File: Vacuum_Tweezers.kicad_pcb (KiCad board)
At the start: 2 copper layers, 40.2 x 28 mm, 0 parts

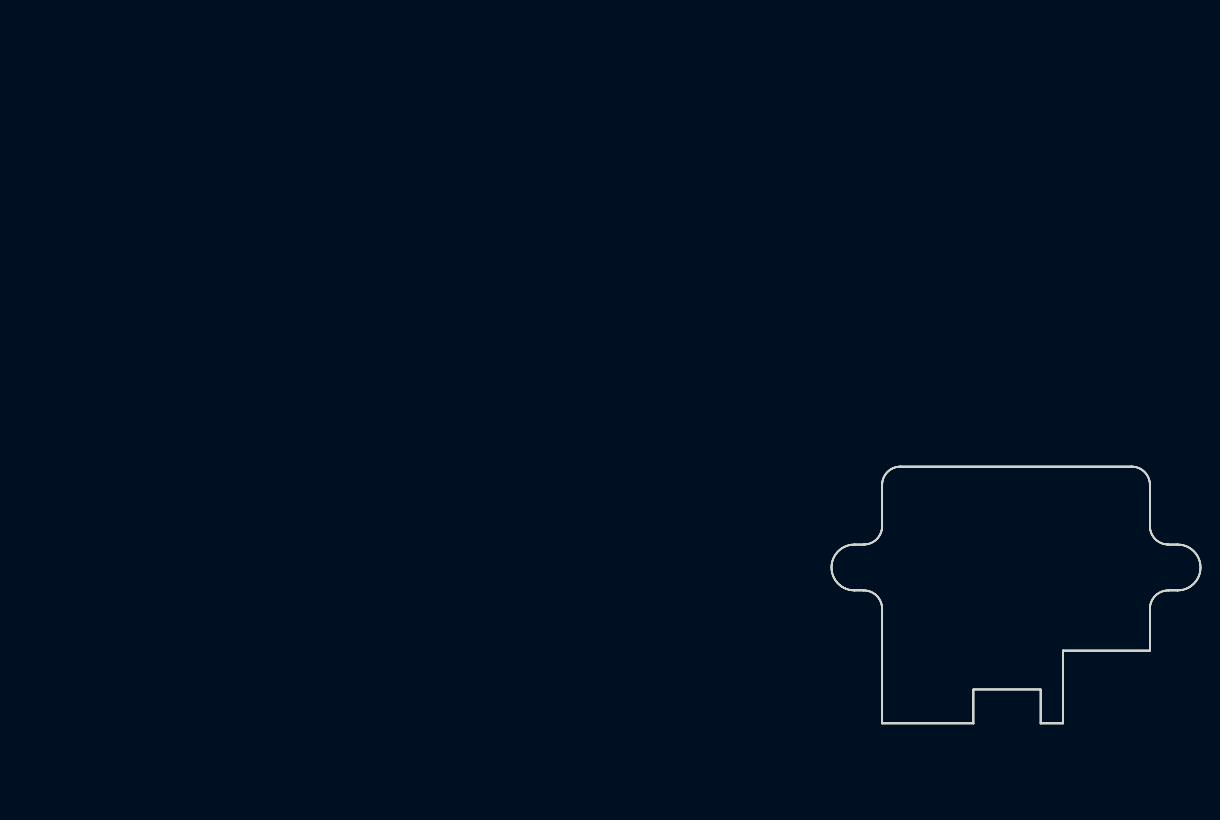
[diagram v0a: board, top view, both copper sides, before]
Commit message: Changed footprints
Modified some footprints to better fit layout and part availability
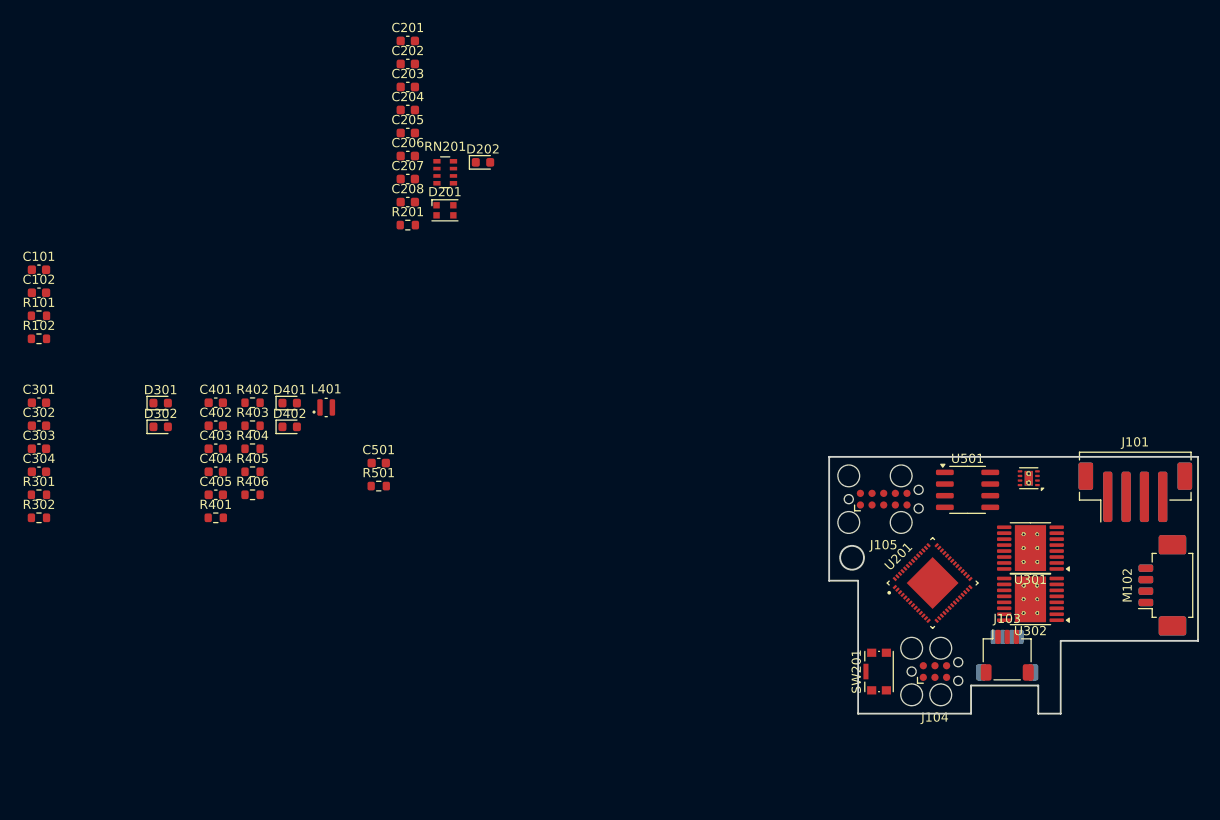
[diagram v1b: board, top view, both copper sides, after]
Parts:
- added C101: 1u, Capacitor_SMD:C_0603_1608Metric, F.Cu at (38.9, 66.2)
- added C102: 1u, Capacitor_SMD:C_0603_1608Metric, F.Cu at (38.9, 68.7)
- added C201: 1u, Capacitor_SMD:C_0603_1608Metric, F.Cu at (79.2, 41.2)
- added C202: 1u, Capacitor_SMD:C_0603_1608Metric, F.Cu at (79.2, 43.7)
- added C203: 1u, Capacitor_SMD:C_0603_1608Metric, F.Cu at (79.2, 46.2)
- added C204: 1u, Capacitor_SMD:C_0603_1608Metric, F.Cu at (79.2, 48.7)
- added C205: 1u, Capacitor_SMD:C_0603_1608Metric, F.Cu at (79.2, 51.3)
- added C206: 1u, Capacitor_SMD:C_0603_1608Metric, F.Cu at (79.2, 53.8)
- added C207: 1u, Capacitor_SMD:C_0603_1608Metric, F.Cu at (79.2, 56.3)
- added C208: 1u, Capacitor_SMD:C_0603_1608Metric, F.Cu at (79.2, 58.8)
- added C301: 10u, Capacitor_SMD:C_0603_1608Metric, F.Cu at (38.9, 80.7)
- added C302: 10u, Capacitor_SMD:C_0603_1608Metric, F.Cu at (38.9, 83.2)
- added C303: 2u2, Capacitor_SMD:C_0603_1608Metric, F.Cu at (38.9, 85.7)
- added C304: 2u2, Capacitor_SMD:C_0603_1608Metric, F.Cu at (38.9, 88.2)
- added C401: 10u, Capacitor_SMD:C_0603_1608Metric, F.Cu at (58.2, 80.7)
- added C402: 10u, Capacitor_SMD:C_0603_1608Metric, F.Cu at (58.2, 83.2)
- added C403: 10u, Capacitor_SMD:C_0603_1608Metric, F.Cu at (58.2, 85.7)
- added C404: 1u, Capacitor_SMD:C_0603_1608Metric, F.Cu at (58.2, 88.2)
- added C405: 1u, Capacitor_SMD:C_0603_1608Metric, F.Cu at (58.2, 90.7)
- added C501: 1u, Capacitor_SMD:C_0603_1608Metric, F.Cu at (76.0, 87.2)
- added D201: WS2812B, LED_SMD:LED_WS2812B-2020_PLCC4_2.0x2.0mm, F.Cu at (83.2, 59.7)
- added D202: LED, Diode_SMD:D_0603_1608Metric, F.Cu at (87.4, 54.5)
- added D301: RED, Diode_SMD:D_0603_1608Metric, F.Cu at (52.2, 80.7)
- added D302: RED, Diode_SMD:D_0603_1608Metric, F.Cu at (52.2, 83.3)
- added D401: RED, LED_SMD:LED_0603_1608Metric, F.Cu at (66.3, 80.7)
- added D402: RED, LED_SMD:LED_0603_1608Metric, F.Cu at (66.3, 83.3)
- added J101: PnP Interface, Connector_JST:JST_PH_B4B-PH-SM4-TB_1x04-1MP_P2.00mm_Vertical, F.Cu at (158.5, 90.4)
- added J102: Magnetic Encoder, Connector_JST:JST_SH_SM04B-SRSS-TB_1x04-1MP_P1.00mm_Horizontal, B.Cu at (144.5, 108.2)
- added J103: Limit Switch, Connector_JST:JST_SH_SM03B-SRSS-TB_1x03-1MP_P1.00mm_Horizontal, F.Cu at (144.5, 108.2)
- added J104: TC2030 PROG, Connector:Tag-Connect_TC2030-IDC-FP_2x03_P1.27mm_Vertical, F.Cu at (136.7, 110.0)
- added J105: TC2050 JTAG, Connector:Tag-Connect_TC2050-IDC-FP_2x05_P1.27mm_Vertical, F.Cu at (131.1, 91.2)
- added J106: PnP Interface, Connector_JST:JST_PH_B4B-PH-SM4-TB_1x04-1MP_P2.00mm_Vertical, B.Cu at (158.5, 90.4)
- added L401: 2u2, Inductor_SMD:L_Coilcraft_XFL2010, F.Cu at (70.3, 81.2)
- added M101: Z-Axis, Connector_Molex:Molex_PicoBlade_53261-0471_1x04-1MP_P1.25mm_Horizontal, B.Cu at (162.1, 100.6)
- added M102: C-Axis, Connector_Molex:Molex_PicoBlade_53261-0471_1x04-1MP_P1.25mm_Horizontal, F.Cu at (162.1, 100.6)
- added R101: 100R, Resistor_SMD:R_0603_1608Metric, F.Cu at (38.9, 71.2)
- added R102: 100R, Resistor_SMD:R_0603_1608Metric, F.Cu at (38.9, 73.7)
- added R201: 1k, Resistor_SMD:R_0603_1608Metric, F.Cu at (79.2, 61.3)
- added R301: 1k, Resistor_SMD:R_0603_1608Metric, F.Cu at (38.9, 90.7)
- added R302: 1k, Resistor_SMD:R_0603_1608Metric, F.Cu at (38.9, 93.2)
- added R401: 100k, Resistor_SMD:R_0603_1608Metric, F.Cu at (58.2, 93.2)
- added R402: 100R, Resistor_SMD:R_0603_1608Metric, F.Cu at (62.2, 80.7)
- added R403: 1k, Resistor_SMD:R_0603_1608Metric, F.Cu at (62.2, 83.2)
- added R404: 3k0, Resistor_SMD:R_0603_1608Metric, F.Cu at (62.2, 85.7)
- added R405: 1k, Resistor_SMD:R_0603_1608Metric, F.Cu at (62.2, 88.2)
- added R406: 430R, Resistor_SMD:R_0603_1608Metric, F.Cu at (62.2, 90.7)
- added R501: 120R, Resistor_SMD:R_0603_1608Metric, F.Cu at (76.0, 89.8)
- added RN201: 10k, Resistor_SMD:R_Array_Convex_4x0603, F.Cu at (83.2, 55.5)
- added SW201: SW_Push, Button_Switch_SMD:SW_Push_1P1T-SH_NO_CK_KMR2xxG, F.Cu at (130.6, 110.0)
- added U201: ESP32-S3-PICO-1-N8R2, SL_ST Tweezers:PQFN40P700X700X106-57N, F.Cu at (136.4, 100.3)
- added U301: DRV8833PWP, Package_SO:HTSSOP-16-1EP_4.4x5mm_P0.65mm_EP3.4x5mm_Mask2.46x2.31mm_ThermalVias, F.Cu at (147.1, 96.5)
- added U302: DRV8833PWP, Package_SO:HTSSOP-16-1EP_4.4x5mm_P0.65mm_EP3.4x5mm_Mask2.46x2.31mm_ThermalVias, F.Cu at (147.1, 102.1)
- added U401: TPS62160DSG, Package_SON:WSON-8-1EP_2x2mm_P0.5mm_EP0.9x1.6mm_ThermalVias, F.Cu at (146.9, 88.9)
- added U501: MAX3078E, Package_SO:SOIC-8_3.9x4.9mm_P1.27mm, F.Cu at (140.2, 90.2)
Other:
- outline, holes or cut-outs redrawn

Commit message: Finished Rev A1 PCB
Added all components and routed parts for Rev A1 PCB
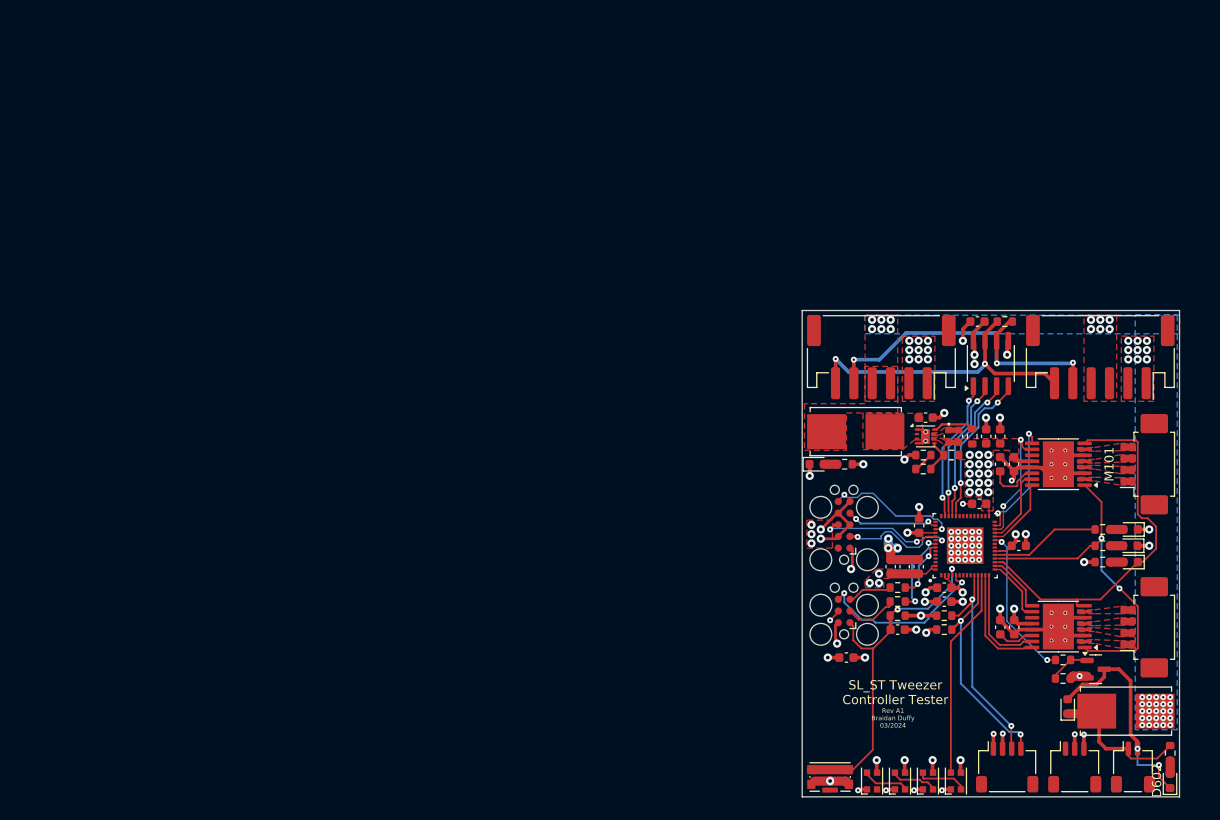
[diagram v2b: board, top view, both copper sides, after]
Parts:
- removed C404, C405: 1u, Capacitor_SMD:C_0603_1608Metric
- removed D402: RED, LED_SMD:LED_0603_1608Metric
- removed R406: 430R, Resistor_SMD:R_0603_1608Metric
- removed RN201: 10k, Resistor_SMD:R_Array_Convex_4x0603
- added D202: C-Axis, LED_SMD:LED_WS2812B-2020_PLCC4_2.0x2.0mm, F.Cu at (135.9, 121.9)
- added D203: Z-Axis, LED_SMD:LED_WS2812B-2020_PLCC4_2.0x2.0mm, F.Cu at (132.8, 121.9)
- added D204: Comms, LED_SMD:LED_WS2812B-2020_PLCC4_2.0x2.0mm, F.Cu at (129.8, 121.9)
- added D601: SM4007L, Diode_SMD:D_0603_1608Metric, F.Cu at (151.1, 113.8)
- added D602: Red, LED_SMD:LED_0603_1608Metric, F.Cu at (162.3, 121.9)
- added F401: 1A5, Fuse:Fuseholder_Littelfuse_Nano2_154x, F.Cu at (128.0, 83.8)
- added F601: 1A, Fuse:Fuseholder_Littelfuse_Nano2_154x, F.Cu at (157.5, 114.3)
- added J107: Valve Coil, Connector_JST:JST_SH_SM02B-SRSS-TB_1x02-1MP_P1.00mm_Horizontal, F.Cu at (158.2, 120.4)
- added Q601: AO3400A, Package_TO_SOT_SMD:SOT-23, F.Cu at (154.2, 109.7)
- added R201: 1k, Resistor_SMD:R_0603_1608Metric, F.Cu at (132.6, 103.9)
- added R202: 1k, Resistor_SMD:R_0603_1608Metric, F.Cu at (137.7, 103.9)
- added R203: 1k, Resistor_SMD:R_0603_1608Metric, F.Cu at (137.7, 105.4)
- added R601: 220R, Resistor_SMD:R_0603_1608Metric, F.Cu at (150.6, 108.7)
- added R602: 10k, Resistor_SMD:R_0603_1608Metric, F.Cu at (150.6, 110.7)
- added R603: 3k0, Resistor_SMD:R_0603_1608Metric, F.Cu at (162.3, 118.9)
- D201: value WS2812B -> Status
- D205: renamed from D202; value LED -> Blue; footprint Diode_SMD:D_0603_1608Metric -> LED_SMD:LED_0603_1608Metric
- D301, D302: footprint Diode_SMD:D_0603_1608Metric -> LED_SMD:LED_0603_1608Metric
- J101: footprint Connector_JST:JST_PH_B4B-PH-SM4-TB_1x04-1MP_P2.00mm_Vertical -> Connector_JST:JST_PH_S6B-PH-SM4-TB_1x06-1MP_P2.00mm_Horizontal
- J102, M101: moved to F.Cu
- J106: footprint Connector_JST:JST_PH_B4B-PH-SM4-TB_1x04-1MP_P2.00mm_Vertical -> Connector_JST:JST_PH_S6B-PH-SM4-TB_1x06-1MP_P2.00mm_Horizontal; moved to F.Cu
- moved R301 116.2 mm to (154.9, 98.0), turned to 180 degrees
- moved R302 116.0 mm to (154.9, 96.3), turned to 180 degrees
- moved C301 109.1 mm to (145.3, 105.2), turned to -90 degrees
- moved D301 107.2 mm to (158.0, 98.0), turned to 180 degrees
- moved D302 106.5 mm to (157.9, 96.3), turned to 180 degrees
- moved C302 106.4 mm to (145.3, 87.4), turned to -90 degrees
- moved C304 106.2 mm to (143.8, 105.2), turned to 90 degrees
- moved C303 104.8 mm to (143.8, 87.4), turned to 90 degrees
- moved R101 98.7 mm to (132.6, 102.3), turned to 180 degrees
- moved C101 97.7 mm to (127.0, 108.5)
- moved C102 97.6 mm to (131.8, 98.6), turned to 90 degrees
- moved R102 97.5 mm to (132.6, 100.8), turned to 180 degrees
- moved C402 85.5 mm to (143.8, 84.3), turned to 90 degrees
- moved C403 84.0 mm to (142.2, 84.3), turned to 90 degrees
- moved D201 83.5 mm to (138.9, 121.9), turned to 90 degrees
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- renumbered R201 to R204
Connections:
- C401 pad 1: VBUS -> /Power Supply/VBUS_P
- D201 pad 2: unconnected-(D201-DOUT-Pad2) -> Net-(D201-DOUT)
- D301 pad 2: /Stepper Drivers/LED_A -> Net-(D301-A)
- D302 pad 2: /Stepper Drivers/LED_A -> Net-(D302-A)
- J101 pad 1: unconnected-(J101-Pin_1-Pad1) -> GND
- J101 pad 2: unconnected-(J101-Pin_2-Pad2) -> GND
- J101 pad 4: GND -> VBUS
- J106 pad 2: VBUS -> GND
- J106 pad 4: /RS_485+ -> VBUS
- M101 pad 1: /Stepper Drivers/Z_AXIS_AOUT2 -> /Stepper Drivers/Z_AXIS_AOUT1
- M101 pad 2: /Stepper Drivers/Z_AXIS_AOUT1 -> /Stepper Drivers/Z_AXIS_AOUT2
- M101 pad 3: /Stepper Drivers/Z_AXIS_BOUT1 -> /Stepper Drivers/Z_AXIS_BOUT2
- M101 pad 4: /Stepper Drivers/Z_AXIS_BOUT2 -> /Stepper Drivers/Z_AXIS_BOUT1
- M102 pad 1: /Stepper Drivers/C_AXIS_AOUT2 -> /Stepper Drivers/C_AXIS_AOUT1
- M102 pad 2: /Stepper Drivers/C_AXIS_AOUT1 -> /Stepper Drivers/C_AXIS_AOUT2
- M102 pad 3: /Stepper Drivers/C_AXIS_BOUT1 -> /Stepper Drivers/C_AXIS_BOUT2
- M102 pad 4: /Stepper Drivers/C_AXIS_BOUT2 -> /Stepper Drivers/C_AXIS_BOUT1
- R301 pad 1: /Stepper Drivers/LED_A -> Net-(D301-A)
- R302 pad 1: /Stepper Drivers/LED_A -> Net-(D302-A)
- U201 pad 12: /Stepper Drivers/~{MTR_SLEEP} -> /Microcontroller/NEO_DATA
- U201 pad 13: /Stepper Drivers/~{MTR_FAULT} -> /Microcontroller/C_AXIS_AIN1
- U201 pad 14: /Microcontroller/Z_AXIS_AIN1 -> /Microcontroller/C_AXIS_AIN2
- U201 pad 15: /Microcontroller/Z_AXIS_AIN2 -> /Microcontroller/C_AXIS_BIN2
- U201 pad 16: /Microcontroller/Z_AXIS_BIN1 -> /Microcontroller/C_AXIS_BIN1
- U201 pad 17: /Microcontroller/Z_AXIS_BIN2 -> /Stepper Drivers/~{MTR_FAULT}
- U201 pad 18: /Microcontroller/ACT_LED -> /Stepper Drivers/~{MTR_SLEEP}
- U201 pad 19: /Microcontroller/NEO_DATA -> /Microcontroller/ACT_LED
- U201 pad 23: /Microcontroller/C_AXIS_AIN1 -> /Microcontroller/VALVE_CTRL
- U201 pad 24: /Microcontroller/C_AXIS_AIN2 -> /Microcontroller/Z_AXIS_AIN1
- U201 pad 25: /Microcontroller/C_AXIS_BIN1 -> /Microcontroller/Z_AXIS_AIN2
- U201 pad 26: /Microcontroller/C_AXIS_BIN2 -> /Microcontroller/Z_AXIS_BIN2
- U201 pad 27: unconnected-(U201-GPIO21-Pad27) -> /Microcontroller/Z_AXIS_BIN1
- U201 pad 38: /Communications/~{RE} -> /Communications/DI
- U201 pad 39: /Communications/RO -> /Communications/DE
- U201 pad 40: /Communications/DI -> /Communications/~{RE}
- U201 pad 41: /Communications/DE -> /Communications/RO
- U401 pad 2: VBUS -> /Power Supply/VBUS_P
- U401 pad 3: VBUS -> /Power Supply/VBUS_P
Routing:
- net GND: track 0.00 -> 89.1 mm, vias 0 -> 78
- net +3V3: track 0.00 -> 51.8 mm, vias 0 -> 38
- net /Stepper Drivers/~{MTR_FAULT}: track 0.00 -> 42.0 mm
- net /Stepper Drivers/~{MTR_SLEEP}: track 0.00 -> 38.9 mm, vias 0 -> 2
- net /RS_485+: track 0.00 -> 38.7 mm, vias 0 -> 3
- net /Microcontroller/~{EN}: track 0.00 -> 38.4 mm, vias 0 -> 2
- net /RS_485-: track 0.00 -> 33.6 mm, vias 0 -> 2
- net /SCL: track 0.00 -> 25.7 mm, vias 0 -> 2
- net /SDA: track 0.00 -> 24.9 mm, vias 0 -> 2
- net /Solenoid Driver/COIL_NEG: track 0.00 -> 24.1 mm, vias 0 -> 2
- net /Microcontroller/NEO_DATA: track 0.00 -> 22.9 mm
- net /Microcontroller/GPIO0: track 0.00 -> 19.0 mm, vias 0 -> 2
- net /Communications/DI: track 0.00 -> 17.0 mm, vias 0 -> 2
- net /Microcontroller/VALVE_CTRL: track 0.00 -> 16.8 mm, vias 0 -> 2
- net /Solenoid Driver/COIL_POS: track 0.00 -> 16.4 mm
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- added copper zone on F.Cu, net +3V3
- added copper zone on In1.Cu, net +3V3
- added copper zone on F.Cu, net /Power Supply/VBUS_P
- added copper zone on F.Cu, net /Stepper Drivers/C_AXIS_AOUT1
- added copper zone on F.Cu, net /Stepper Drivers/C_AXIS_AOUT2
- added copper zone on F.Cu, net /Stepper Drivers/C_AXIS_BOUT1
- added copper zone on F.Cu, net /Stepper Drivers/C_AXIS_BOUT2
- added copper zone on F.Cu, net /Stepper Drivers/Z_AXIS_AOUT1
- added copper zone on F.Cu, net /Stepper Drivers/Z_AXIS_AOUT2
- added copper zone on F.Cu, net /Stepper Drivers/Z_AXIS_BOUT1
- added copper zone on F.Cu, net /Stepper Drivers/Z_AXIS_BOUT2
- added copper zone on F.Cu, net GND
- added copper zone on In2.Cu, net GND
- added copper zone on F.Cu, net Net-(U401-SW)
- added copper zone on B.Cu, net VBUS
- added copper zone on F.Cu, net VBUS
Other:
- board size 40.2 x 28 mm -> 41.1 x 53 mm
- copper layers 2 -> 4
- rule pad_to_mask_clearance: 0 -> 0.08
- board text added: "Rev A1 Braidan Duffy 03/2024"
- board text added: "SL_ST Tweezer Controller Tester"
